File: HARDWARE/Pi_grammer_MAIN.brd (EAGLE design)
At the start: 81.3 x 78.7 mm, 31 parts, among them J2 TARGET_copy, J3 TESTBED, J4 CABLE, U1 AT42QT1010SOT23

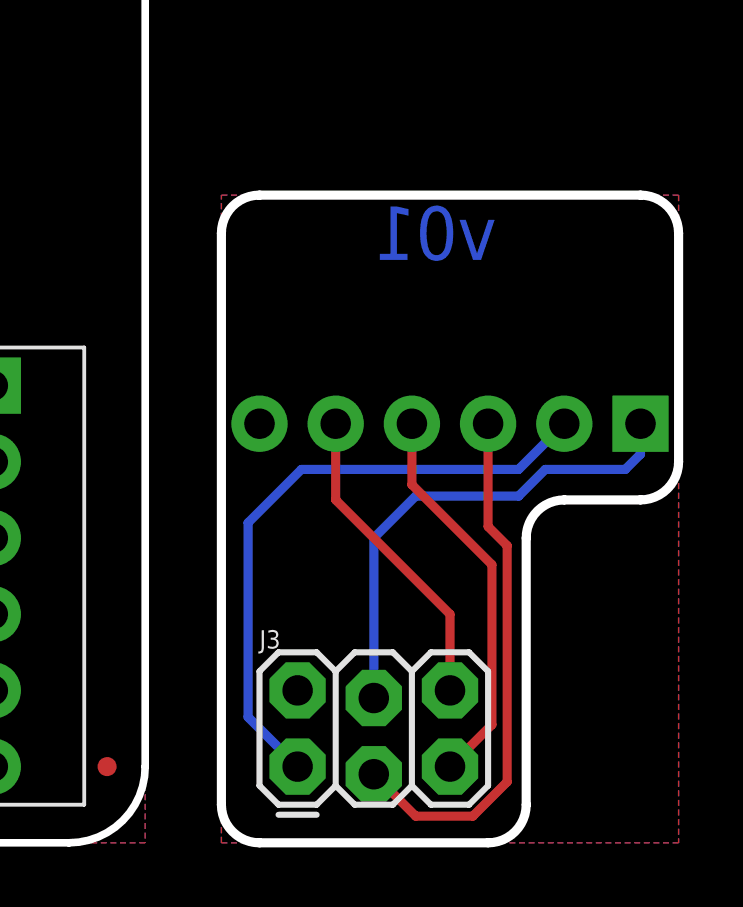
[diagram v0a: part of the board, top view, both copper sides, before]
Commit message: Split design into MAIN and ADAPTER
The original eagle file contained both PCBs for this project. As
requested by production, I split them out into separate design files -
for ease of CAMing and ordering.
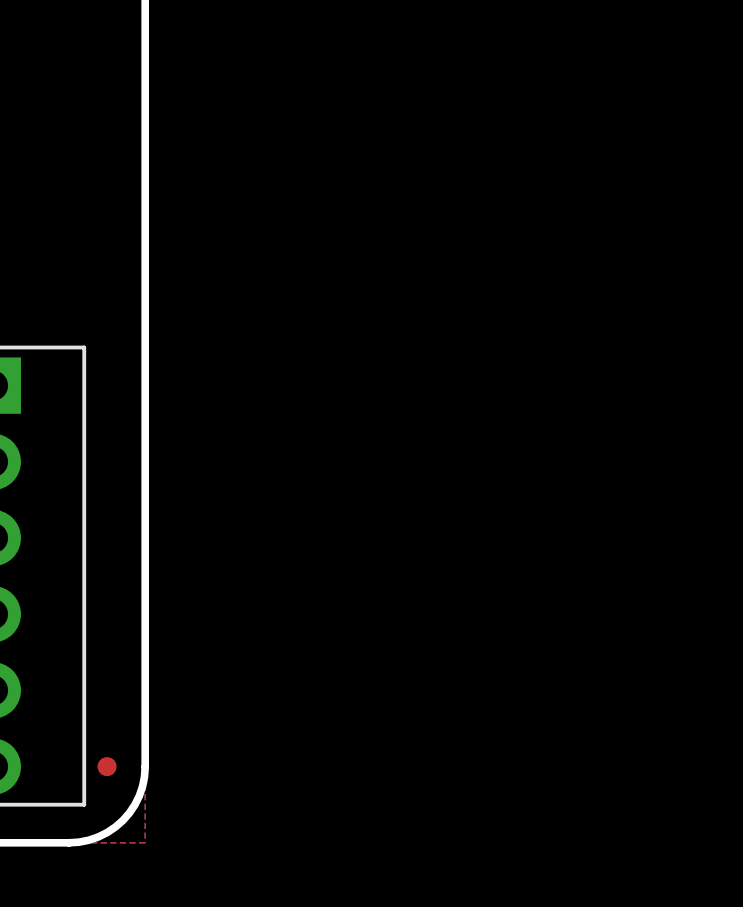
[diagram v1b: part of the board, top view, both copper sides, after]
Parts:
- removed J3: TESTBED, SparkFun-Connectors:2X3_LOCK
- removed J4: CABLE, SparkFun-Connectors:MOLEX-1X6-RA
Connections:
- removed net GND_C: J3.6, J4.5
- removed net MISO_C: J3.1, J4.2
- removed net MOSI_C: J3.4, J4.1
- removed net RST_C: J3.5, J4.4
- removed net SCK_C: J3.3, J4.3
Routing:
- net MISO_C: track 20.7 -> 0.00 mm
- net SCK_C: track 17.7 -> 0.00 mm
- net MOSI_C: track 16.4 -> 0.00 mm
- net RST_C: track 13.1 -> 0.00 mm
- net GND_C: track 10.5 -> 0.00 mm
- removed copper zone on layer 1, net GND_C
- removed copper zone on layer 16, net GND_C
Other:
- board size 81.3 x 78.7 mm -> 63.5 x 78.7 mm
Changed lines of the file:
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@@
 <text x="54.61" y="5.08" size="0.6096" layer="21" font="vector" ratio="15" align="center">GND</text>
 <text x="54.61" y="2.54" size="0.6096" layer="21" font="vector" ratio="15" align="center">NC</text>
-<wire x1="76.2" y1="1.27" x2="74.93" y2="0" width="0.3048" layer="20" curve="-90"/>
-<wire x1="74.93" y1="0" x2="67.31" y2="0" width="0.3048" layer="20"/>
-<wire x1="67.31" y1="0" x2="66.04" y2="1.27" width="0.3048" layer="20" curve="-90"/>
-<wire x1="66.04" y1="1.27" x2="66.04" y2="20.32" width="0.3048" layer="20"/>
-<wire x1="66.04" y1="20.32" x2="67.31" y2="21.59" width="0.3048" layer="20" curve="-90"/>
-<wire x1="67.31" y1="21.59" x2="80.01" y2="21.59" width="0.3048" layer="20"/>
-<wire x1="80.01" y1="21.59" x2="81.28" y2="20.32" width="0.3048" layer="20" curve="-90"/>
-<wire x1="81.28" y1="20.32" x2="81.28" y2="12.7" width="0.3048" layer="20"/>
-<wire x1="81.28" y1="12.7" x2="80.01" y2="11.43" width="0.3048" layer="20" curve="-90"/>
-<wire x1="80.01" y1="11.43" x2="77.47" y2="11.43" width="0.3048" layer="20"/>
-<wire x1="77.47" y1="11.43" x2="76.2" y2="10.16" width="0.3048" layer="20" curve="90"/>
-<wire x1="76.2" y1="10.16" x2="76.2" y2="1.27" width="0.3048" layer="20"/>
 <text x="52.07" y="-21.59" size="1.778" layer="51" font="vector">Pete Lewis</text>
-<text x="71.12" y="20.32" size="1.778" layer="16" font="vector" ratio="21" rot="MR0" align="center-right">v01</text>
 </plain>
 <attributes>
@@
 <attribute name="PROD_ID" value="CONN-09698" x="58.42" y="15.24" size="1.778" layer="27" rot="R270" display="off"/>
 </element>
-<element name="J3" library="SparkFun-Connectors" package="2X3_LOCK" value="TESTBED" x="68.58" y="2.54">
-<attribute name="PROD_ID" value="CONN-11566" x="68.58" y="2.54" size="1.778" layer="27" display="off"/>
-</element>
-<element name="J4" library="SparkFun-Connectors" package="MOLEX-1X6-RA" value="CABLE" x="80.01" y="13.97" rot="MR0">
-<attribute name="PROD_ID" value="CONN-10140" x="80.01" y="13.97" size="1.778" layer="28" rot="MR0" display="off"/>
-</element>
 <element name="FRAME1" library="SparkFun-Aesthetics" package="CREATIVE_COMMONS" value="FRAME-LETTER" x="21.59" y="-21.59"/>
 <element name="FD1" library="SparkFun-Aesthetics" package="FIDUCIAL-MICRO" value="FIDUCIALUFIDUCIAL" x="2.54" y="76.2"/>
@@
 <via x="53.0225" y="44.45" extent="1-16" drill="0.508"/>
 </signal>
-<signal name="MOSI_C">
-<contactref element="J4" pad="1"/>
-<contactref element="J3" pad="4"/>
-<wire x1="80.01" y1="13.97" x2="80.01" y2="12.954" width="0.3048" layer="16"/>
-<wire x1="80.01" y1="12.954" x2="79.502" y2="12.446" width="0.3048" layer="16"/>
-<wire x1="79.502" y1="12.446" x2="76.835" y2="12.446" width="0.3048" layer="16"/>
-<wire x1="76.835" y1="12.446" x2="75.946" y2="11.557" width="0.3048" layer="16"/>
-<wire x1="75.946" y1="11.557" x2="72.517" y2="11.557" width="0.3048" layer="16"/>
-<wire x1="72.517" y1="11.557" x2="71.12" y2="10.16" width="0.3048" layer="16"/>
-<wire x1="71.12" y1="10.16" x2="71.12" y2="4.826" width="0.3048" layer="16"/>
-</signal>
-<signal name="MISO_C">
-<contactref element="J4" pad="2"/>
-<contactref element="J3" pad="1"/>
-<wire x1="77.47" y1="13.97" x2="75.946" y2="12.446" width="0.3048" layer="16"/>
-<wire x1="75.946" y1="12.446" x2="68.707" y2="12.446" width="0.3048" layer="16"/>
-<wire x1="68.707" y1="12.446" x2="66.929" y2="10.668" width="0.3048" layer="16"/>
-<wire x1="66.929" y1="10.668" x2="66.929" y2="4.191" width="0.3048" layer="16"/>
-<wire x1="66.929" y1="4.191" x2="68.58" y2="2.54" width="0.3048" layer="16"/>
-</signal>
-<signal name="SCK_C">
-<contactref element="J3" pad="3"/>
-<contactref element="J4" pad="3"/>
-<wire x1="74.93" y1="13.97" x2="74.93" y2="10.541" width="0.3048" layer="1"/>
-<wire x1="74.93" y1="10.541" x2="75.565" y2="9.906" width="0.3048" layer="1"/>
-<wire x1="75.565" y1="9.906" x2="75.565" y2="2.032" width="0.3048" layer="1"/>
-<wire x1="75.565" y1="2.032" x2="74.422" y2="0.889" width="0.3048" layer="1"/>
-<wire x1="74.422" y1="0.889" x2="72.517" y2="0.889" width="0.3048" layer="1"/>
-<wire x1="72.517" y1="0.889" x2="71.12" y2="2.286" width="0.3048" layer="1"/>
-</signal>
-<signal name="RST_C">
-<contactref element="J4" pad="4"/>
-<contactref element="J3" pad="5"/>
-<wire x1="72.39" y1="13.97" x2="72.39" y2="11.938" width="0.3048" layer="1"/>
-<wire x1="75.057" y1="9.271" x2="75.057" y2="3.937" width="0.3048" layer="1"/>
-<wire x1="75.057" y1="3.937" x2="73.66" y2="2.54" width="0.3048" layer="1"/>
-<wire x1="72.39" y1="11.938" x2="75.057" y2="9.271" width="0.3048" layer="1"/>
-</signal>
-<signal name="GND_C">
-<contactref element="J4" pad="5"/>
-<contactref element="J3" pad="6"/>
-<wire x1="69.85" y1="13.97" x2="69.85" y2="11.43" width="0.3048" layer="1"/>
-<polygon width="0.3048" layer="16" isolate="0.3048">
-<vertex x="81.28" y="0"/>
-<vertex x="66.04" y="0"/>
-<vertex x="66.04" y="21.59"/>
-<vertex x="81.28" y="21.59"/>
-</polygon>
-<polygon width="0.3048" layer="1" isolate="0.3048">
-<vertex x="81.28" y="0"/>
-<vertex x="66.04" y="0"/>
-<vertex x="66.04" y="21.59"/>
-<vertex x="81.28" y="21.59"/>
-</polygon>
-<wire x1="69.85" y1="11.43" x2="73.66" y2="7.62" width="0.3048" layer="1"/>
-<wire x1="73.66" y1="7.62" x2="73.66" y2="5.08" width="0.3048" layer="1"/>
-</signal>
 </signals>
